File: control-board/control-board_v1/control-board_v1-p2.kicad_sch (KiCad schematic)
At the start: 29 parts, among them U2 AD77x8, Y1 32kHz

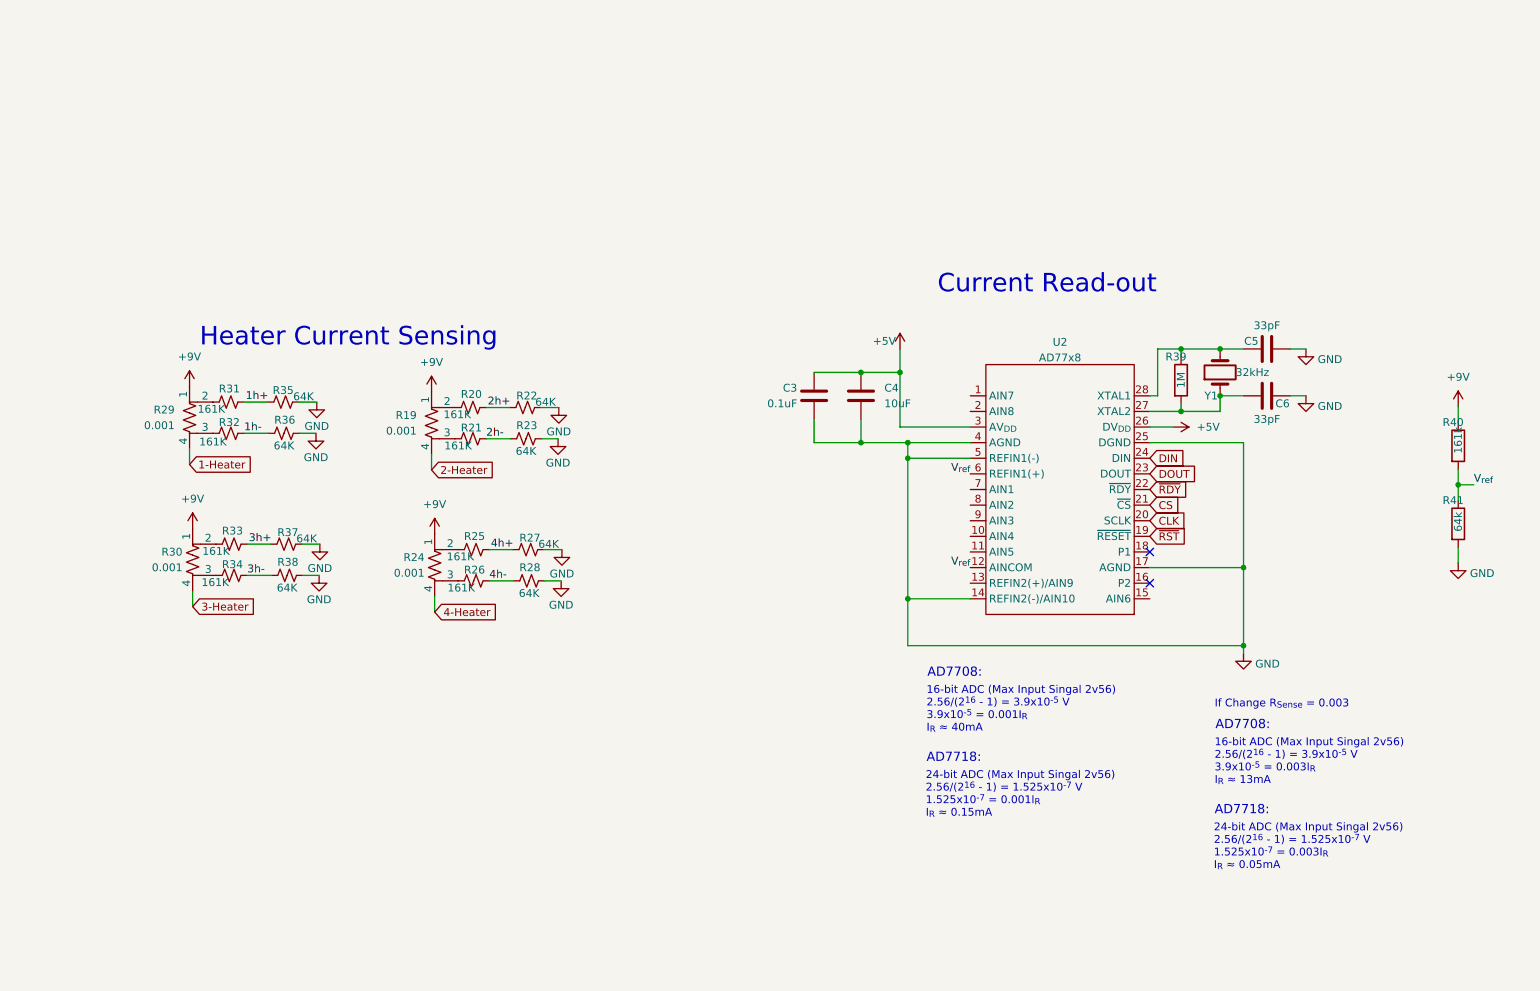
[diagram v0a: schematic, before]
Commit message: added opamp to reduce adc signals
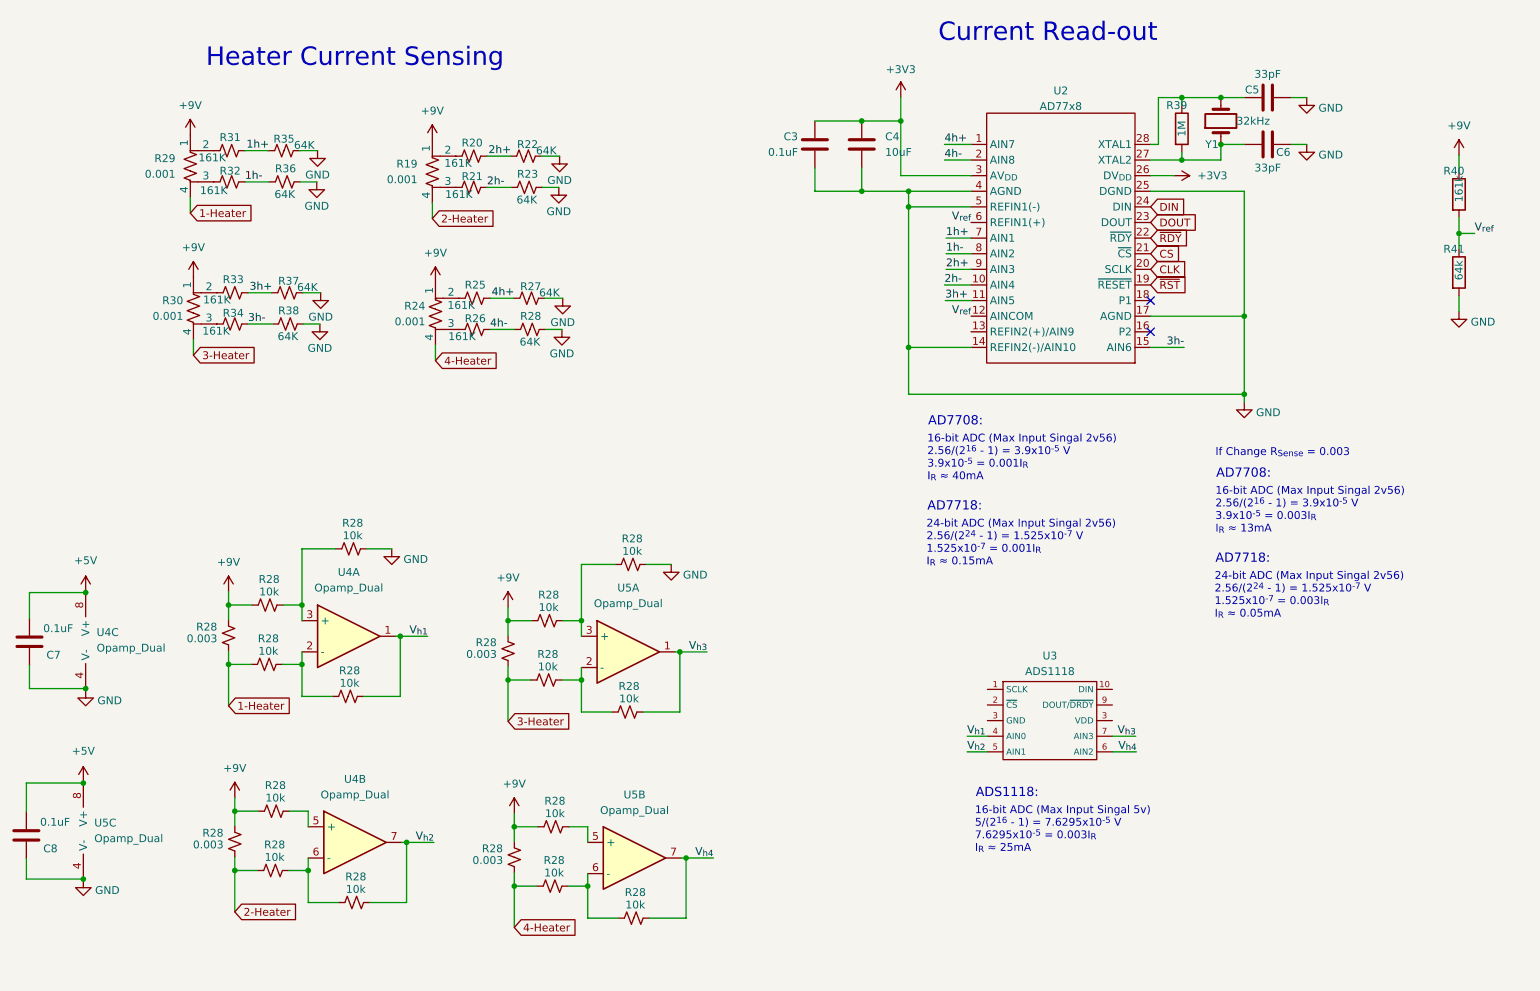
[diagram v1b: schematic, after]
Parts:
- added C7, C8: 0.1uF, Capacitor_SMD:C_0603_1608Metric_Pad1.08x0.95mm_HandSolder, symbol Device:C
- added R28 (x14): 10k, Resistor_SMD:R_0805_2012Metric, symbol Device:R_Small_US
- added R28 (x4): 0.003, Resistor_SMD:R_0805_2012Metric, symbol Device:R_Small_US
- added U3: ADS1118, symbol Analog_ADC:ADS1118
- added U4, U5: Opamp_Dual, symbol Device:Opamp_Dual
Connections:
- net +5V: now also C7.1, C8.1, U4.8 (V+), U5.8 (V+); no longer C3.1, C4.1, U2.26 (DV_{DD}), U2.3 (AV_{DD})
- net +9V: now also R28.2, R28.2, R28.2, R28.2, R28.2, R28.2, R28.2, R28.2
- net 1-Heater: now also R28.1, R28.2
- net 1h+: now also U2.7 (AIN1)
- net 1h-: now also U2.8 (AIN2)
- net 2-Heater: now also R28.1, R28.2
- net 2h+: now also U2.9 (AIN3)
- net 2h-: now also U2.10 (AIN4)
- net 3-Heater: now also R28.1, R28.2
- net 3h+: now also U2.11 (AIN5)
- net 3h-: now also U2.15 (AIN6)
- net 4-Heater: now also R28.1, R28.2
- net 4h+: now also U2.1 (AIN7)
- net 4h-: now also U2.2 (AIN8)
- net GND: now also C7.2, C8.2, R28.1, R28.1, U4.4 (V-), U5.4 (V-)
- new net: R28.1, U5.5 (+)
- new net: R28.1, R28.2, U4.2 (-)
- new net: R28.1, R28.2, U4.3 (+)
- new net: R28.1, R28.2, U5.3 (+)
- new net: R28.1, R28.2, U5.2 (-)
- new net: R28.1, U4.5 (+)
- new net: R28.1, R28.2, U4.6 (-)
- new net: R28.1, R28.2, U5.6 (-)
- new net +3V3: C3.1, C4.1, U2.26 (DV_{DD}), U2.3 (AV_{DD})
- new net V_{h1}: R28.1, U3.4 (AIN0), U4.1
- new net V_{h2}: R28.1, U3.5 (AIN1), U4.7
- new net V_{h3}: R28.1, U3.7 (AIN3), U5.1
- new net V_{h4}: R28.1, U3.6 (AIN2), U5.7
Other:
- note added: "16-bit ADC (Max Input Singal 5v) 5/(2^{16} - 1) = 7.6295x10^{-5} V 7.6295x10^{-5} = 0.003I_{R} I_{R} ≈ 25mA"
- note added: "24-bit ADC (Max Input Singal 2v56) 2.56/(2^{24} - 1) = 1.525x10^{-7} V 1.525x10^{-7} = 0.001I_{R} I_{R} ≈ 0.15mA"
- note added: "24-bit ADC (Max Input Singal 2v56) 2.56/(2^{24} - 1) = 1.525x10^{-7} V 1.525x10^{-7} = 0.003I_{R} I_{R} ≈ 0.05mA"
- note added: "ADS1118:"
- note removed: "24-bit ADC (Max Input Singal 2v56) 2.56/(2^{16} - 1) = 1.525x10^{-7} V 1.525x10^{-7} = 0.001I_{R} I_{R} ≈ 0.15mA"
- note removed: "24-bit ADC (Max Input Singal 2v56) 2.56/(2^{16} - 1) = 1.525x10^{-7} V 1.525x10^{-7} = 0.003I_{R} I_{R} ≈ 0.05mA"
- moved on the sheet: C3, C4, C5, C6, R19, R20, R21, R22, R23, R24, R25, R26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

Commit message: added gain op-amp
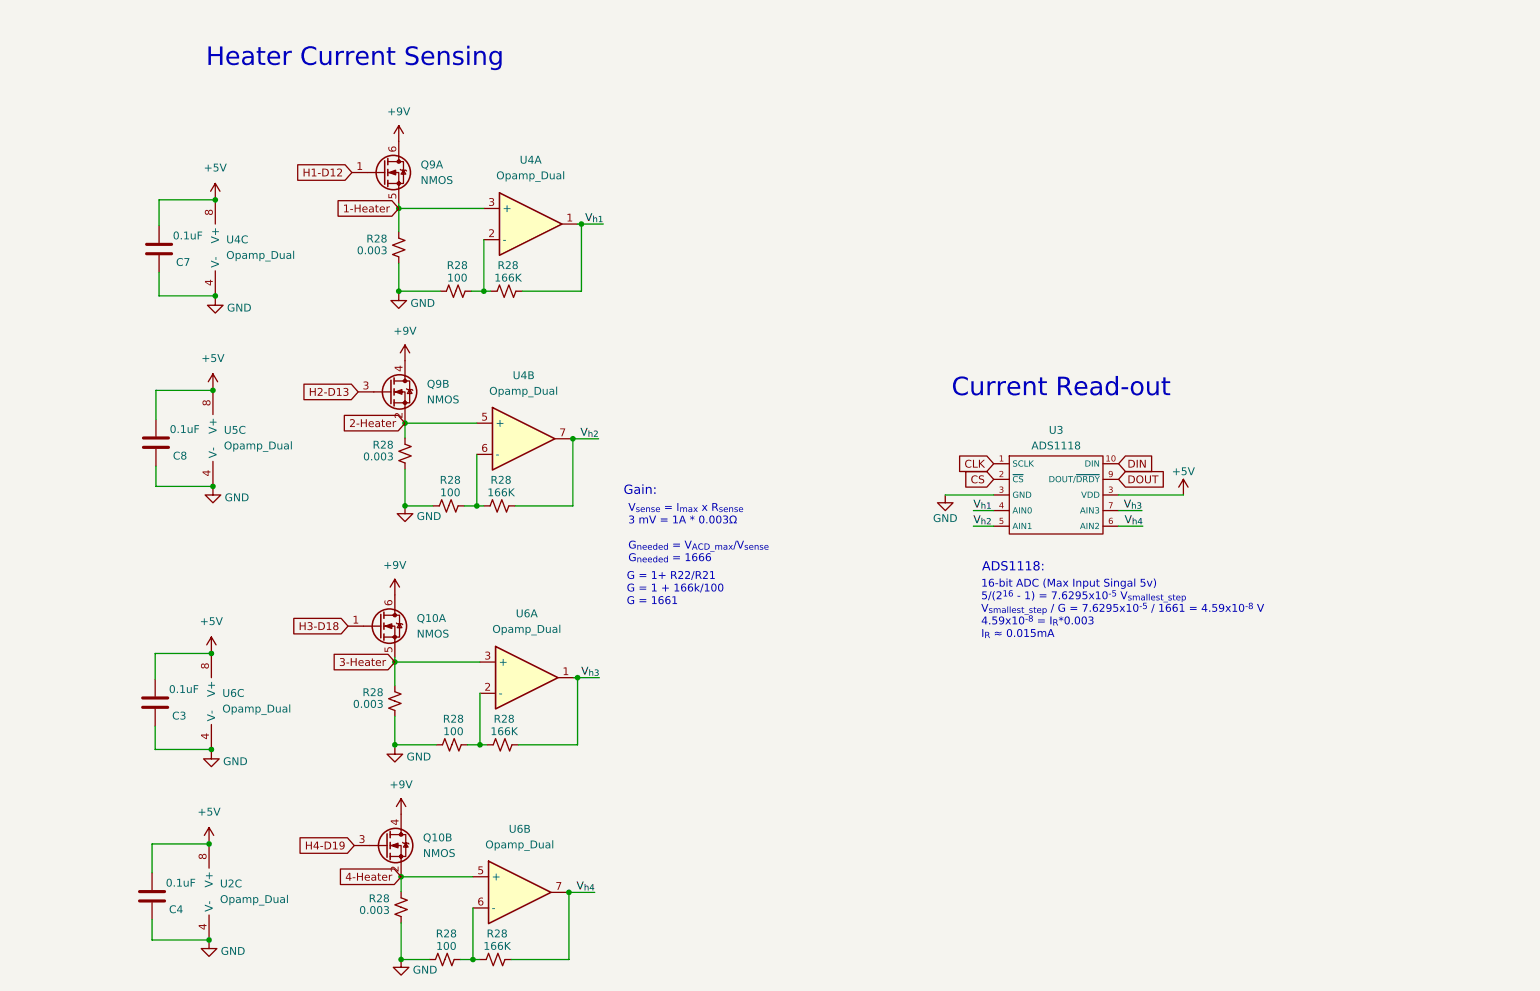
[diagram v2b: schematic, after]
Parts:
- removed C5, C6: 33pF, Capacitor_SMD:C_0805_2012Metric_Pad1.18x1.45mm_HandSolder, symbol Device:C
- removed R19, R24, R29, R30: 0.001, symbol Device:R_Shunt_US
- removed R20, R21, R25, R26, R31, R32, R33, R34: 161K, Resistor_SMD:R_0805_2012Metric, symbol Device:R_Small_US
- removed R22, R23, R27, R28, R35, R36, R37, R38: 64K, Resistor_SMD:R_0805_2012Metric, symbol Device:R_Small_US
- removed R28 (x14): 10k, Resistor_SMD:R_0805_2012Metric, symbol Device:R_Small_US
- removed R28 (x2): 0.003, Resistor_SMD:R_0805_2012Metric, symbol Device:R_Small_US
- removed R39: 1M, Resistor_SMD:R_0805_2012Metric_Pad1.20x1.40mm_HandSolder, symbol Device:R
- removed R40: 161k, Resistor_SMD:R_0805_2012Metric_Pad1.20x1.40mm_HandSolder, symbol Device:R
- removed R41: 64k, Resistor_SMD:R_0805_2012Metric_Pad1.20x1.40mm_HandSolder, symbol Device:R
- removed U2: AD77x8, Package_SO:SOIC-28W_7.5x18.7mm_P1.27mm, symbol unl_silab:AD77x8
- removed unit 1 of U5
- removed unit 2 of U5
- removed Y1: 32kHz, Crystal:Crystal_SMD_3215-2Pin_3.2x1.5mm, symbol Device:Crystal
- added Q10, Q9: NMOS, symbol Device:Q_Dual_NMOS_G1S2G2D2S1D1
- added R28 (x4): 166K, Resistor_SMD:R_0805_2012Metric, symbol Device:R_Small_US
- added R28 (x4): 100, Resistor_SMD:R_0805_2012Metric, symbol Device:R_Small_US
- added R28 (x2): 0.003, Resistor_SMD:R_0805_2012Metric, symbol Device:R_Small_US
- added U2, U6: Opamp_Dual, symbol Device:Opamp_Dual
- C3: footprint Capacitor_SMD:C_0805_2012Metric_Pad1.18x1.45mm_HandSolder -> Capacitor_SMD:C_0603_1608Metric_Pad1.08x0.95mm_HandSolder; LCSC (none) -> C314282
- C4: value 10uF -> 0.1uF; footprint Capacitor_SMD:C_0805_2012Metric_Pad1.18x1.45mm_HandSolder -> Capacitor_SMD:C_0603_1608Metric_Pad1.08x0.95mm_HandSolder; LCSC (none) -> C314282
- R28: PartNum (none) -> CSS2H-2512K-3L00F
- U3: PartNum (none) -> ADS1118IDGSR
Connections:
- net +3V3 is gone; now on net +5V: C3.1, C4.1
- net +5V: now also U3.3 (VDD), U2.8 (V+), U6.8 (V+)
- net +9V: now also Q10.4 (D), Q10.6 (D), Q9.4 (D), Q9.6 (D); no longer R28.2, R28.2
- net 1-Heater: now also R28.2, U4.3 (+), Q9.5 (S); no longer R28.1
- net 2-Heater: now also R28.2, U4.5 (+), Q9.2 (S); no longer R28.1
- net 3-Heater: now also Q10.5 (S), R28.2, U6.3 (+)
- net 4-Heater: now also Q10.2 (S), R28.2, U6.5 (+)
- net CLK: now also U3.1 (SCLK)
- net CS: now also U3.2 (~{CS})
- net DIN: now also U3.10 (DIN)
- net DOUT: now also U3.9 (DOUT/~{DRDY})
- net GND: now also R28.1, R28.1, U3.3 (VDD), R28.1, R28.1, R28.2, R28.2, R28.2, R28.2, U2.4 (V-), U6.4 (V-)
- net V_{h1}: now also R28.1
- net V_{h2}: now also R28.1
- net V_{h3}: now also R28.1, U6.1
- net V_{h4}: now also R28.1, U6.7
- net at U4.2 (-): now also R28.1, R28.2
- net at U4.6 (-): now also R28.1, R28.2
- new net: R28.1, R28.2, U6.2 (-)
- new net: R28.1, R28.2, U6.6 (-)
- new net H1-D12: Q9.1 (G)
- new net H2-D13: Q9.3 (G)
- new net H3-D18: Q10.1 (G)
- new net H4-D19: Q10.3 (G)
- no-connect marks 2 -> 0
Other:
- note added: "16-bit ADC (Max Input Singal 5v) 5/(2^{16} - 1) = 7.6295x10^{-5} V_{smallest_step} V_{smallest_step} / G = 7.6295x10^{-5} / 1661 = 4.59x10^{-8} V 4.59x10^{-8} = I_{R}*0.003 I_{R} ≈ 0.015mA"
- note added: "G = 1+ R22/R21 G = 1 + 166k/100 G = 1661"
- note added: "Gain:"
- note added: "V_{sense} = I_{max} x R_{sense} 3 mV = 1A * 0.003Ω G_{needed} = V_{ACD_max}/V_{sense} G_{needed} = 1666"
- note removed: "16-bit ADC (Max Input Singal 2v56) 2.56/(2^{16} - 1) = 3.9x10^{-5} V 3.9x10^{-5} = 0.001I_{R} I_{R} ≈ 40mA"
- note removed: "16-bit ADC (Max Input Singal 2v56) 2.56/(2^{16} - 1) = 3.9x10^{-5} V 3.9x10^{-5} = 0.003I_{R} I_{R} ≈ 13mA"
- note removed: "16-bit ADC (Max Input Singal 5v) 5/(2^{16} - 1) = 7.6295x10^{-5} V 7.6295x10^{-5} = 0.003I_{R} I_{R} ≈ 25mA"
- note removed: "24-bit ADC (Max Input Singal 2v56) 2.56/(2^{24} - 1) = 1.525x10^{-7} V 1.525x10^{-7} = 0.001I_{R} I_{R} ≈ 0.15mA"
- note removed: "24-bit ADC (Max Input Singal 2v56) 2.56/(2^{24} - 1) = 1.525x10^{-7} V 1.525x10^{-7} = 0.003I_{R} I_{R} ≈ 0.05mA"
- note removed: "AD7708:"
- note removed: "AD7718:"
- note removed: "If Change R_{Sense} = 0.003"
- moved on the sheet: C7, C8, R28, U3, U4A, U4B, U4C, U5C

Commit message: fixed footprint matching
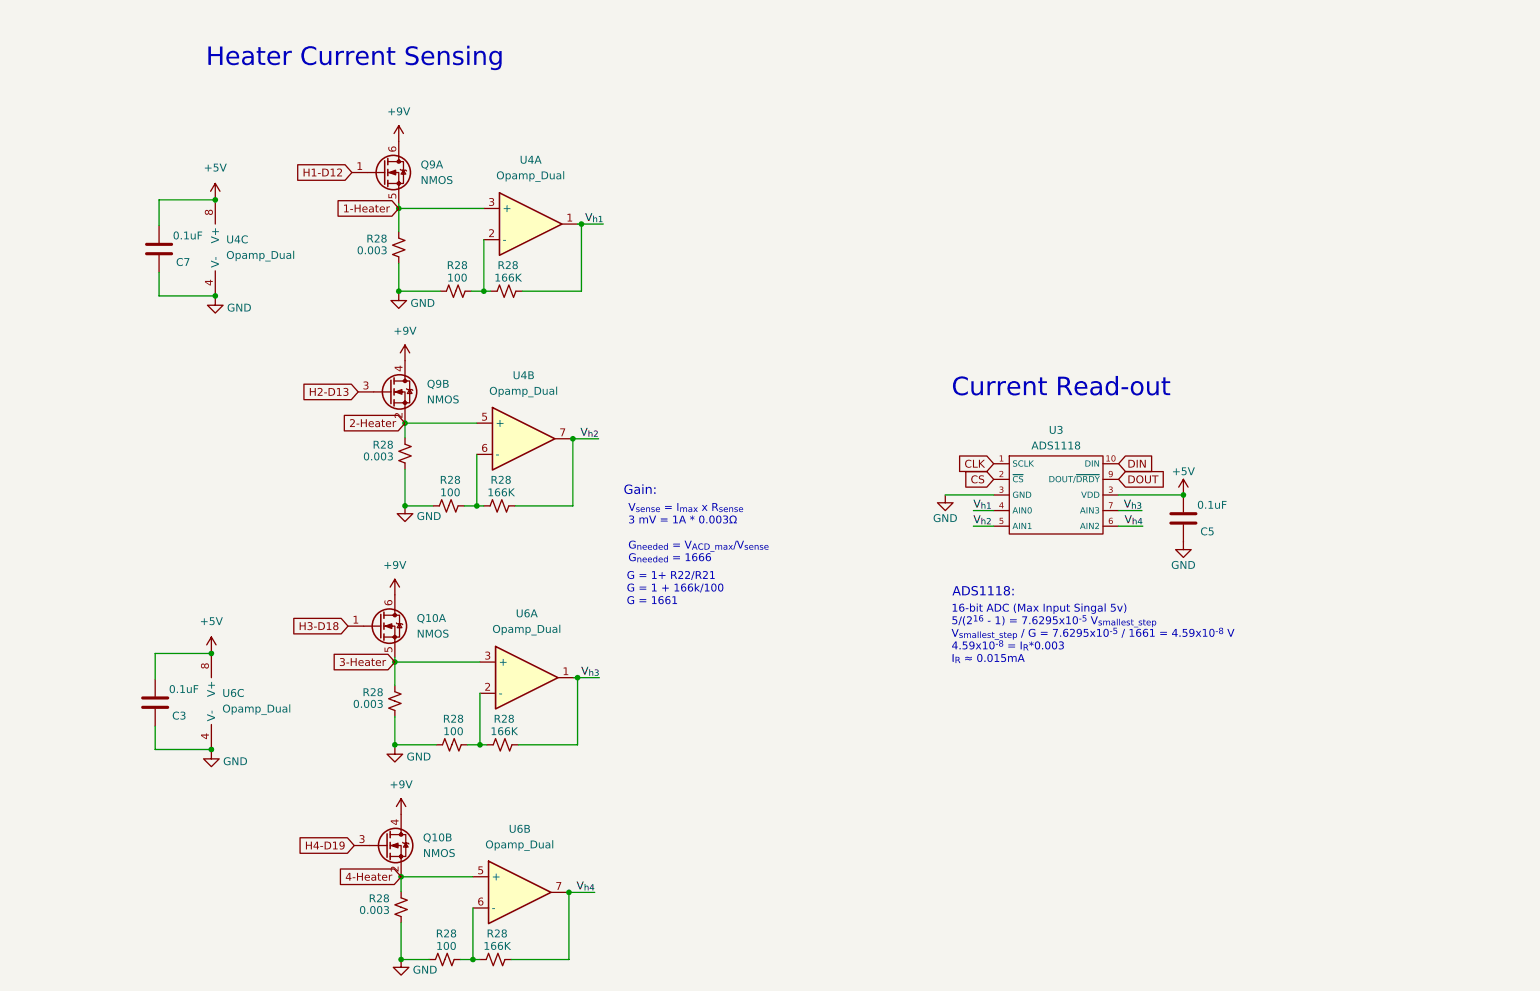
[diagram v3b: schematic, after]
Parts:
- removed C4, C8: 0.1uF, Capacitor_SMD:C_0603_1608Metric_Pad1.08x0.95mm_HandSolder, symbol Device:C
- removed U2, U5: Opamp_Dual, symbol Device:Opamp_Dual
- added C5: 0.1uF, Capacitor_SMD:C_0805_2012Metric, symbol Device:C
- C3, C7: footprint Capacitor_SMD:C_0603_1608Metric_Pad1.08x0.95mm_HandSolder -> Capacitor_SMD:C_0805_2012Metric
- Q10, Q9: footprint (none) -> Package_TO_SOT_SMD:SOT-23-6
- R28: footprint Resistor_SMD:R_0805_2012Metric -> Resistor_SMD:R_2512_6332Metric
- U3: footprint (none) -> Package_SO:VSSOP-10_3x3mm_P0.5mm
- U4, U6: footprint (none) -> LED_SMD:LED_0603_1608Metric; PartNum (none) -> MCP6487T-E/SN
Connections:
- net +5V: now also C5.1
- net GND: now also C5.2

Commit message: added pcb layout
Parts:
- U4, U6: footprint LED_SMD:LED_0603_1608Metric -> Package_SO:SOIC-8_3.9x4.9mm_P1.27mm
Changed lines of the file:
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@@
       (effects (font (size 1.27 1.27)))
     )
-    (property "Footprint" "LED_SMD:LED_0603_1608Metric" (at 108.331 51.943 0)
+    (property "Footprint" "Package_SO:SOIC-8_3.9x4.9mm_P1.27mm" (at 108.331 51.943 0)
       (effects (font (size 1.27 1.27)) hide)
     )
@@
       (effects (font (size 1.27 1.27)))
     )
-    (property "Footprint" "LED_SMD:LED_0603_1608Metric" (at 107.188 86.868 0)
+    (property "Footprint" "Package_SO:SOIC-8_3.9x4.9mm_P1.27mm" (at 107.188 86.868 0)
       (effects (font (size 1.27 1.27)) hide)
     )
@@
       (effects (font (size 1.27 1.27)))
     )
-    (property "Footprint" "LED_SMD:LED_0603_1608Metric" (at 107.696 125.73 0)
+    (property "Footprint" "Package_SO:SOIC-8_3.9x4.9mm_P1.27mm" (at 107.696 125.73 0)
       (effects (font (size 1.27 1.27)) hide)
     )
@@
       (effects (font (size 1.27 1.27)) (justify left))
     )
-    (property "Footprint" "LED_SMD:LED_0603_1608Metric" (at 58.928 129.54 0)
+    (property "Footprint" "Package_SO:SOIC-8_3.9x4.9mm_P1.27mm" (at 58.928 129.54 0)
       (effects (font (size 1.27 1.27)) hide)
     )
@@
       (effects (font (size 1.27 1.27)) (justify left))
     )
-    (property "Footprint" "LED_SMD:LED_0603_1608Metric" (at 59.563 55.753 0)
+    (property "Footprint" "Package_SO:SOIC-8_3.9x4.9mm_P1.27mm" (at 59.563 55.753 0)
       (effects (font (size 1.27 1.27)) hide)
     )
@@
       (effects (font (size 1.27 1.27)))
     )
-    (property "Footprint" "LED_SMD:LED_0603_1608Metric" (at 106.553 160.655 0)
-      (effects (font (size 1.27 1.27)) hide)
-    )
+    (property "Footprint" "Package_SO:SOIC-8_3.9x4.9mm_P1.27mm" (at 106.553 160.655 0)
+      (effects (font (size 1.27 1.27)) hide)
+    )

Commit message: added datasheets
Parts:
- R28: footprint Resistor_SMD:R_0805_2012Metric -> Resistor_SMD:R_0603_1608Metric
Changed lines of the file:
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@@
       (effects (font (size 1.27 1.27)))
     )
-    (property "Footprint" "Resistor_SMD:R_0805_2012Metric" (at 103.251 97.79 0)
+    (property "Footprint" "Resistor_SMD:R_0603_1608Metric" (at 103.251 97.79 0)
       (effects (font (size 1.27 1.27)) hide)
     )
@@
       (effects (font (size 1.27 1.27)))
     )
-    (property "Footprint" "Resistor_SMD:R_0805_2012Metric" (at 104.394 62.865 0)
+    (property "Footprint" "Resistor_SMD:R_0603_1608Metric" (at 104.394 62.865 0)
       (effects (font (size 1.27 1.27)) hide)
     )
@@
       (effects (font (size 1.27 1.27)))
     )
-    (property "Footprint" "Resistor_SMD:R_0805_2012Metric" (at 103.759 136.652 0)
+    (property "Footprint" "Resistor_SMD:R_0603_1608Metric" (at 103.759 136.652 0)
       (effects (font (size 1.27 1.27)) hide)
     )
@@
       (effects (font (size 1.27 1.27)))
     )
-    (property "Footprint" "Resistor_SMD:R_0805_2012Metric" (at 102.616 171.577 0)
-      (effects (font (size 1.27 1.27)) hide)
-    )
+    (property "Footprint" "Resistor_SMD:R_0603_1608Metric" (at 102.616 171.577 0)
+      (effects (font (size 1.27 1.27)) hide)
+    )
